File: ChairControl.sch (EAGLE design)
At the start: 22 parts, among them J1 Digital_0_7, J2 Analog, J3 Digital_8_13, SW1 TL46WO, X1 INPUT, X2 OUTPUT, X4 INPUT

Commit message: Routing and silkscreen
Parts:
- added R13, R14, R15, R16, R17, R18: 1K, freetronics-jon:RESISTOR0603
- SW1: value TL46WO -> SWITCH-DPDT3; device switch:TL46WO -> freetronics-jon:SWITCH-DPDT3
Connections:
- new net N$2: R1.1, R13.2, R2.2
- new net N$3: R14.2, R3.1, R4.2
- new net N$4: R15.2, R5.1, R6.2
- new net N$7: R16.1, R7.1, R8.2
- new net N$8: R11.1, R17.1, R9.2
- new net N$9: R10.2, R12.1, R18.1
- net A0: now also R13.1; no longer R1.1, R2.2
- net A1: now also R14.1; no longer R3.1, R4.2
- net A2: now also R15.1; no longer R5.1, R6.2
- net A3: now also R16.2; no longer R7.1, R8.2
- net A4: now also R17.2; no longer R11.1, R9.2
- net A5: now also R18.2; no longer R10.2, R12.1
- net DIRECTION_IN: now also SW1.5; no longer SW1.P1
- net DIRECTION_OUT: now also SW1.4; no longer SW1.S1
- net SPEED_IN: now also SW1.2; no longer SW1.P
- net SPEED_OUT: now also SW1.3; no longer SW1.S
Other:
- note added: "(DIRECTION 1)"
- note added: "(DIRECTION 2)"
- note added: "(REFERENCE 1)"
- note added: "(REFERENCE 2)"
- note added: "(SPEED 1)"
- note added: "(SPEED 2)"
- note added: "Add local ATmega328P to drive trainer port? Will the voltage dividers bias the lines enough to cause a problem for the chair? Should we take the samples after the switch, so only if it's isolated? Or maybe add equivalent pull-ups above each line so the input to the voltage divider doesn't pull it down, eg: 2 x 47K in series as pullups Note: ATmega328P analog inputs are optimised for sources with 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"
- note added: "Chair Control Breakout"
- note added: "SKU: CHAIRCONTROL"
- note added: "www.superhouse.tv/chaircontrol"
- note removed: "SH-PROTO-BASIC"
- note removed: "Wheelchair Input Interceptor"
- note removed: "www.superhouse.tv/wheelchairinterceptor"
- moved on the sheet: R1, R10, R11, R12, R2, R3, R4, R5, R6, R9, S1, X2

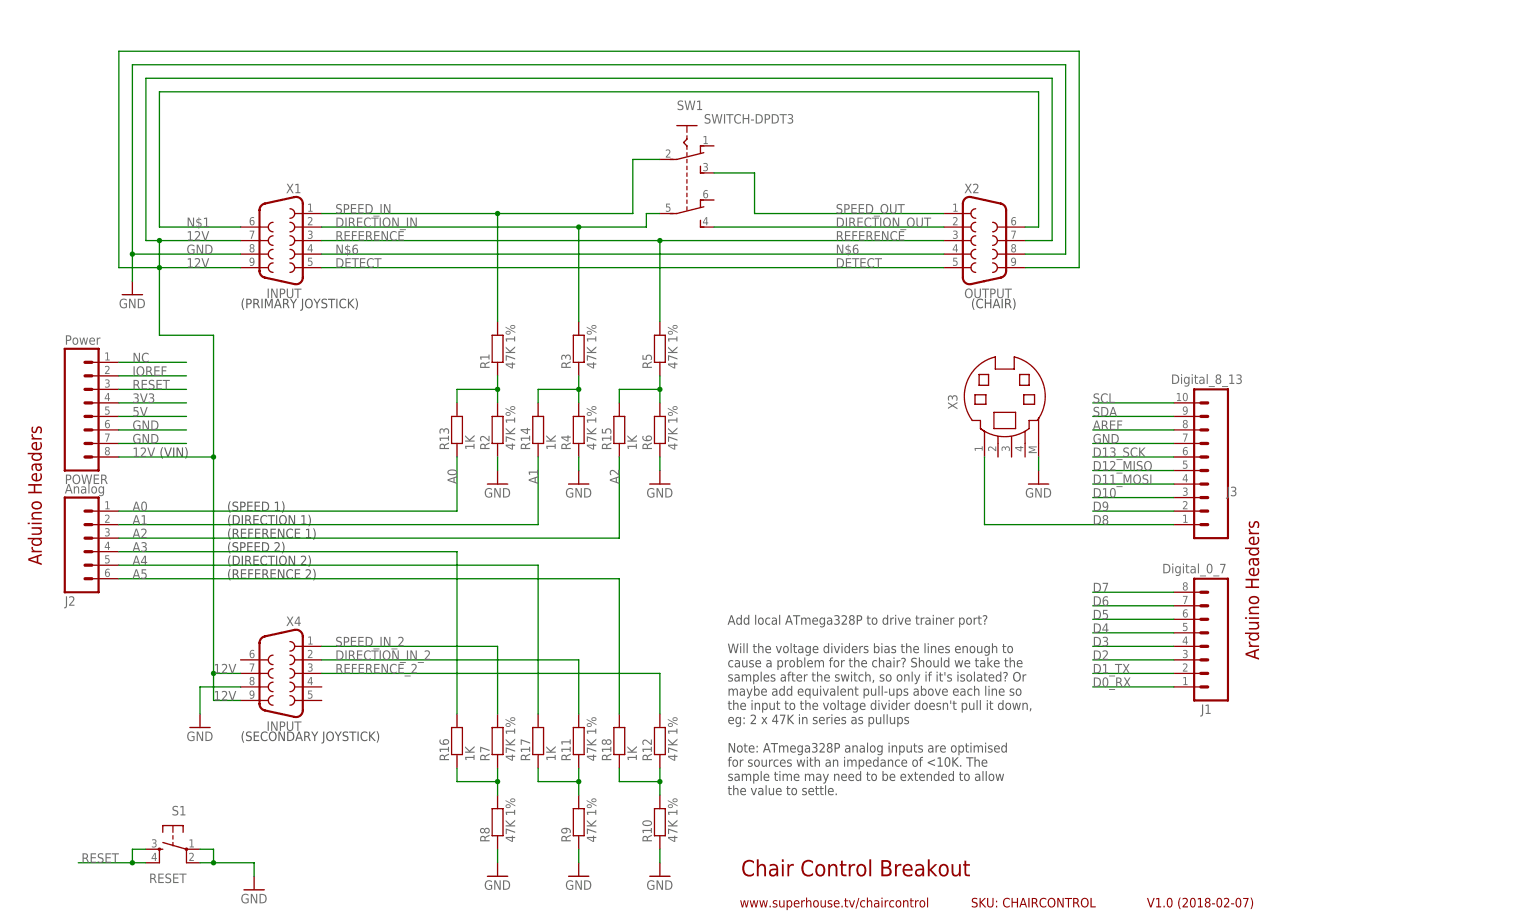
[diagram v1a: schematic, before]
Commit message: Added trim inputs and extra headers for Mega footprint
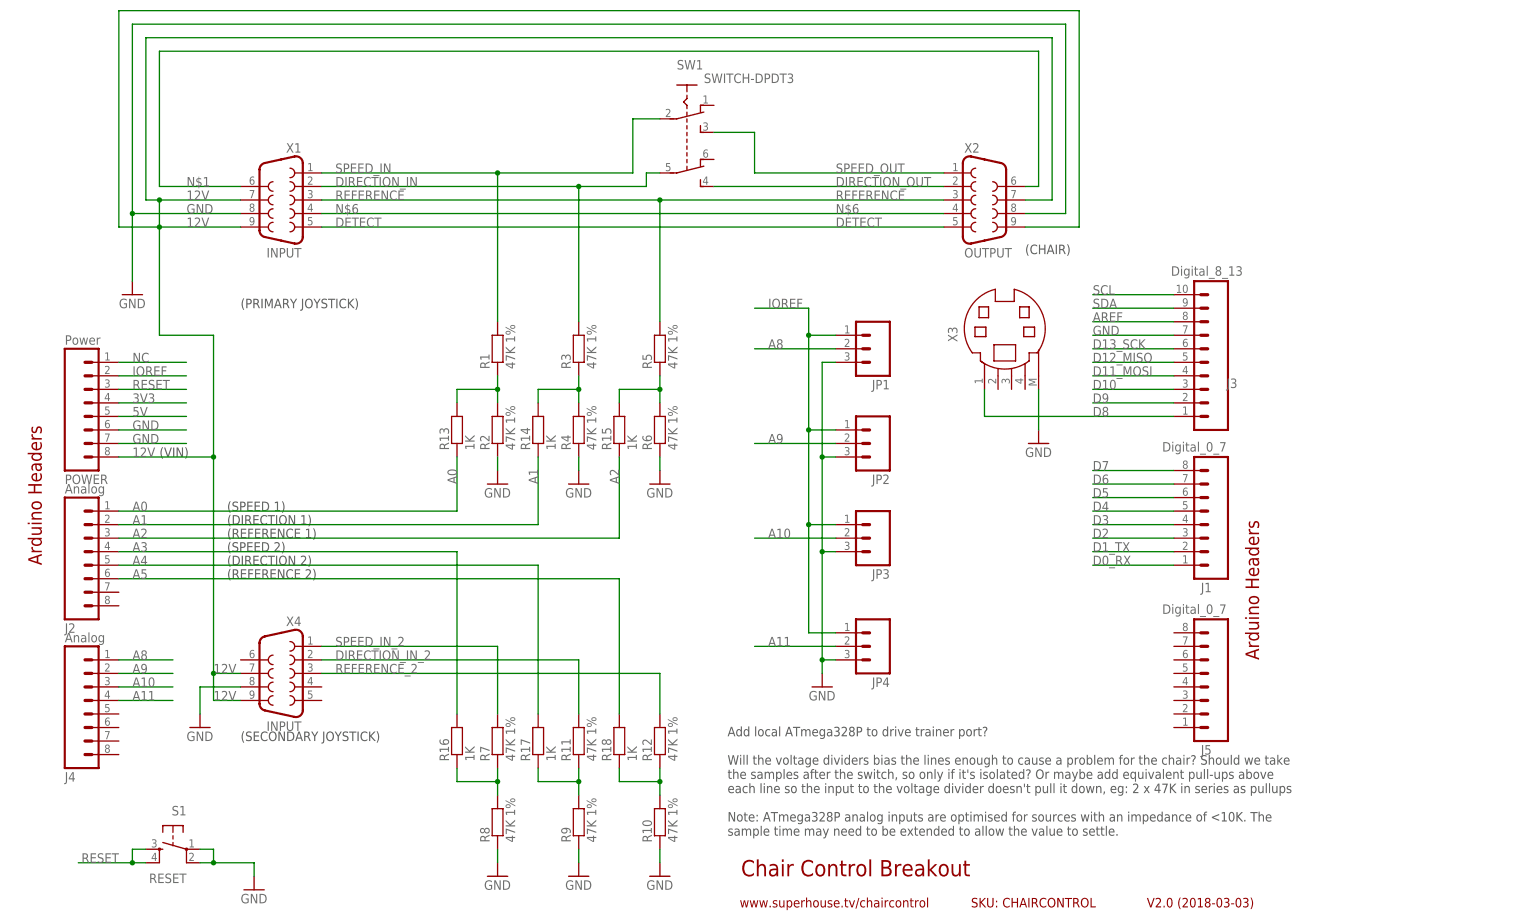
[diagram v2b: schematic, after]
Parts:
- added J4: Analog, freetronics-jon:M08PTH
- added J5: Digital_0_7, freetronics:M08
- added JP1, JP2, JP3, JP4: (no value), freetronics-jon:M03PTH
- J2: device freetronics:M06SIP -> freetronics-jon:M08PTH
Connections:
- new net A10: J4.3, JP3.2
- new net A11: J4.4, JP4.2
- new net A8: J4.1, JP1.2
- new net A9: J4.2, JP2.2
- net GND: now also JP1.3, JP2.3, JP3.3, JP4.3
- net IOREF: now also JP1.1, JP2.1, JP3.1, JP4.1
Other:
- note added: "V2.0 (2018-03-03)"
- note removed: "V1.0 (2018-02-07)"
- moved on the sheet: J1, J3, SW1, X1, X2, X3

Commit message: Isolated 12V power from passthrough to allow separate power source
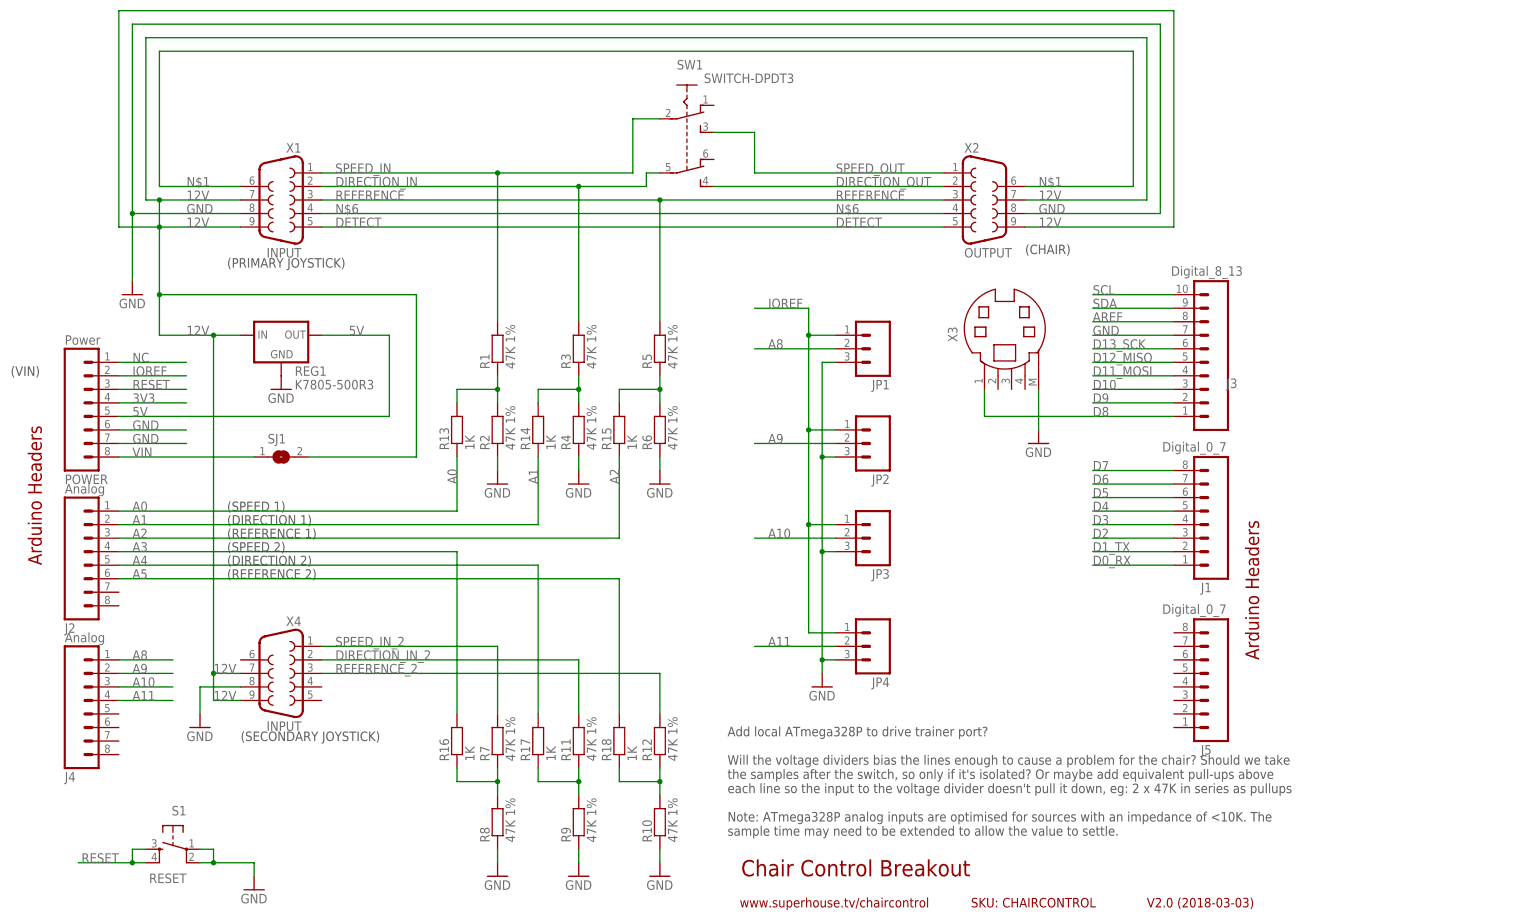
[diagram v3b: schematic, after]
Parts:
- added REG1: K7805-500R3, freetronics-jon:K78XX-500R3
- added SJ1: (no value), freetronics-jon:SJN
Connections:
- new net VIN: POWER.8, SJ1.1
- net 12V: now also REG1.IN, SJ1.2; no longer POWER.8
- net 5V: now also REG1.OUT
- net GND: now also REG1.GND
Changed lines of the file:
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@@
 <?xml version="1.0" encoding="utf-8"?>
 <!DOCTYPE eagle SYSTEM "eagle.dtd">
-<eagle version="8.6.0">
+<eagle version="8.7.0">
 <drawing>
 <settings>
@@
 <part name="GND11" library="freetronics" deviceset="GND" device=""/>
 <part name="J5" library="freetronics" deviceset="M08" device="" value="Digital_0_7"/>
+<part name="REG1" library="freetronics-jon" deviceset="K78XX-500R3" device="" value="K7805-500R3"/>
+<part name="GND12" library="freetronics" deviceset="GND" device=""/>
+<part name="SJ1" library="freetronics-jon" deviceset="SJ" device="N"/>
 </parts>
 <sheets>
@@
 <frame x1="185.42" y1="5.08" x2="218.44" y2="10.16" columns="8" rows="5" layer="94"/>
 <frame x1="218.44" y1="5.08" x2="243.84" y2="10.16" columns="8" rows="5" layer="94"/>
-<text x="50.8" y="119.38" size="1.778" layer="97">(PRIMARY JOYSTICK)</text>
+<text x="48.26" y="127" size="1.778" layer="97">(PRIMARY JOYSTICK)</text>
 <text x="198.12" y="129.54" size="1.778" layer="97">(CHAIR)</text>
-<text x="35.56" y="91.44" size="1.778" layer="97">(VIN)</text>
+<text x="7.62" y="106.68" size="1.778" layer="97">(VIN)</text>
 <text x="50.8" y="38.1" size="1.778" layer="97">(SECONDARY JOYSTICK)</text>
 <text x="142.24" y="20.32" size="1.778" layer="97">Add local ATmega328P to drive trainer port?
@@
 <attribute name="VALUE" x="235.966" y="61.976" size="1.778" layer="96" rot="MR0"/>
 </instance>
+<instance part="REG1" gate="G$1" x="58.42" y="114.3"/>
+<instance part="GND12" gate="1" x="58.42" y="104.14"/>
+<instance part="SJ1" gate="1" x="58.42" y="91.44"/>
 </instances>
 <busses>
@@
 <net name="5V" class="0">
 <segment>
-<wire x1="27.94" y1="99.06" x2="40.64" y2="99.06" width="0.1524" layer="91"/>
 <label x="30.48" y="99.06" size="1.778" layer="95"/>
 <pinref part="POWER" gate="G$1" pin="5"/>
+<pinref part="REG1" gate="G$1" pin="OUT"/>
+<wire x1="66.04" y1="114.3" x2="78.74" y2="114.3" width="0.1524" layer="91"/>
+<wire x1="78.74" y1="114.3" x2="78.74" y2="99.06" width="0.1524" layer="91"/>
+<wire x1="78.74" y1="99.06" x2="27.94" y2="99.06" width="0.1524" layer="91"/>
+<label x="71.12" y="114.3" size="1.778" layer="95"/>
 </segment>
 </net>
@@
 <wire x1="50.8" y1="137.16" x2="30.48" y2="137.16" width="0.1524" layer="91"/>
 <wire x1="30.48" y1="137.16" x2="30.48" y2="172.72" width="0.1524" layer="91"/>
-<wire x1="30.48" y1="172.72" x2="205.74" y2="172.72" width="0.1524" layer="91"/>
-<wire x1="205.74" y1="172.72" x2="205.74" y2="137.16" width="0.1524" layer="91"/>
+<wire x1="30.48" y1="172.72" x2="223.52" y2="172.72" width="0.1524" layer="91"/>
+<wire x1="223.52" y1="172.72" x2="223.52" y2="137.16" width="0.1524" layer="91"/>
 <pinref part="X2" gate="G$1" pin="8"/>
-<wire x1="205.74" y1="137.16" x2="198.12" y2="137.16" width="0.1524" layer="91"/>
+<wire x1="223.52" y1="137.16" x2="198.12" y2="137.16" width="0.1524" layer="91"/>
 <label x="40.64" y="137.16" size="1.778" layer="95"/>
 <pinref part="GND2" gate="1" pin="GND"/>
 <wire x1="30.48" y1="124.46" x2="30.48" y2="137.16" width="0.1524" layer="91"/>
 <junction x="30.48" y="137.16"/>
+<label x="200.66" y="137.16" size="1.778" layer="95"/>
 </segment>
 <segment>
@@
 <wire x1="160.02" y1="109.22" x2="160.02" y2="91.44" width="0.1524" layer="91"/>
 <junction x="160.02" y="91.44"/>
+</segment>
+<segment>
+<pinref part="REG1" gate="G$1" pin="GND"/>
+<pinref part="GND12" gate="1" pin="GND"/>
 </segment>
 </net>
@@
 <wire x1="50.8" y1="142.24" x2="35.56" y2="142.24" width="0.1524" layer="91"/>
 <wire x1="35.56" y1="142.24" x2="35.56" y2="167.64" width="0.1524" layer="91"/>
-<wire x1="35.56" y1="167.64" x2="200.66" y2="167.64" width="0.1524" layer="91"/>
-<wire x1="200.66" y1="167.64" x2="200.66" y2="142.24" width="0.1524" layer="91"/>
+<wire x1="35.56" y1="167.64" x2="218.44" y2="167.64" width="0.1524" layer="91"/>
+<wire x1="218.44" y1="167.64" x2="218.44" y2="142.24" width="0.1524" layer="91"/>
 <pinref part="X2" gate="G$1" pin="6"/>
-<wire x1="200.66" y1="142.24" x2="198.12" y2="142.24" width="0.1524" layer="91"/>
+<wire x1="218.44" y1="142.24" x2="198.12" y2="142.24" width="0.1524" layer="91"/>
 <label x="40.64" y="142.24" size="1.778" layer="95"/>
+<label x="200.66" y="142.24" size="1.778" layer="95"/>
 </segment>
 </net>
@@
 <wire x1="35.56" y1="134.62" x2="27.94" y2="134.62" width="0.1524" layer="91"/>
 <wire x1="27.94" y1="134.62" x2="27.94" y2="175.26" width="0.1524" layer="91"/>
-<wire x1="27.94" y1="175.26" x2="208.28" y2="175.26" width="0.1524" layer="91"/>
-<wire x1="208.28" y1="175.26" x2="208.28" y2="134.62" width="0.1524" layer="91"/>
+<wire x1="27.94" y1="175.26" x2="226.06" y2="175.26" width="0.1524" layer="91"/>
+<wire x1="226.06" y1="175.26" x2="226.06" y2="134.62" width="0.1524" layer="91"/>
 <pinref part="X2" gate="G$1" pin="9"/>
-<wire x1="208.28" y1="134.62" x2="198.12" y2="134.62" width="0.1524" layer="91"/>
+<wire x1="226.06" y1="134.62" x2="198.12" y2="134.62" width="0.1524" layer="91"/>
 <label x="40.64" y="134.62" size="1.778" layer="95"/>
-<wire x1="35.56" y1="134.62" x2="35.56" y2="114.3" width="0.1524" layer="91"/>
+<wire x1="35.56" y1="134.62" x2="35.56" y2="121.92" width="0.1524" layer="91"/>
 <junction x="35.56" y="134.62"/>
+<wire x1="35.56" y1="121.92" x2="35.56" y2="114.3" width="0.1524" layer="91"/>
 <wire x1="35.56" y1="114.3" x2="45.72" y2="114.3" width="0.1524" layer="91"/>
-<wire x1="45.72" y1="114.3" x2="45.72" y2="91.44" width="0.1524" layer="91"/>
-<wire x1="45.72" y1="91.44" x2="27.94" y2="91.44" width="0.1524" layer="91"/>
-<label x="30.48" y="91.44" size="1.778" layer="95"/>
-<pinref part="POWER" gate="G$1" pin="8"/>
-<wire x1="45.72" y1="91.44" x2="45.72" y2="50.8" width="0.1524" layer="91"/>
-<junction x="45.72" y="91.44"/>
+<label x="40.64" y="114.3" size="1.778" layer="95"/>
+<wire x1="45.72" y1="114.3" x2="45.72" y2="50.8" width="0.1524" layer="91"/>
 <pinref part="X4" gate="G$1" pin="9"/>
 <wire x1="45.72" y1="50.8" x2="45.72" y2="45.72" width="0.1524" layer="91"/>
@@
 <wire x1="35.56" y1="139.7" x2="33.02" y2="139.7" width="0.1524" layer="91"/>
 <wire x1="33.02" y1="139.7" x2="33.02" y2="170.18" width="0.1524" layer="91"/>
-<wire x1="33.02" y1="170.18" x2="203.2" y2="170.18" width="0.1524" layer="91"/>
-<wire x1="203.2" y1="170.18" x2="203.2" y2="139.7" width="0.1524" layer="91"/>
+<wire x1="33.02" y1="170.18" x2="220.98" y2="170.18" width="0.1524" layer="91"/>
+<wire x1="220.98" y1="170.18" x2="220.98" y2="139.7" width="0.1524" layer="91"/>
 <pinref part="X2" gate="G$1" pin="7"/>
-<wire x1="203.2" y1="139.7" x2="198.12" y2="139.7" width="0.1524" layer="91"/>
+<wire x1="220.98" y1="139.7" x2="198.12" y2="139.7" width="0.1524" layer="91"/>
 <label x="40.64" y="139.7" size="1.778" layer="95"/>
 <wire x1="35.56" y1="134.62" x2="35.56" y2="139.7" width="0.1524" layer="91"/>
@@
 <label x="45.72" y="50.8" size="1.778" layer="95"/>
 <label x="45.72" y="45.72" size="1.778" layer="95"/>
+<label x="200.66" y="134.62" size="1.778" layer="95"/>
+<label x="200.66" y="139.7" size="1.778" layer="95"/>
+<pinref part="REG1" gate="G$1" pin="IN"/>
+<wire x1="45.72" y1="114.3" x2="50.8" y2="114.3" width="0.1524" layer="91"/>
+<junction x="45.72" y="114.3"/>
+<pinref part="SJ1" gate="1" pin="2"/>
+<wire x1="63.5" y1="91.44" x2="83.82" y2="91.44" width="0.1524" layer="91"/>
+<wire x1="83.82" y1="91.44" x2="83.82" y2="121.92" width="0.1524" layer="91"/>
+<wire x1="83.82" y1="121.92" x2="35.56" y2="121.92" width="0.1524" layer="91"/>
+<junction x="35.56" y="121.92"/>
 </segment>
 </net>
@@
 </segment>
 </net>
+<net name="VIN" class="0">
+<segment>
+<pinref part="POWER" gate="G$1" pin="8"/>
+<label x="30.48" y="91.44" size="1.778" layer="95"/>
+<pinref part="SJ1" gate="1" pin="1"/>
+<wire x1="27.94" y1="91.44" x2="53.34" y2="91.44" width="0.1524" layer="91"/>
+</segment>
+</net>
